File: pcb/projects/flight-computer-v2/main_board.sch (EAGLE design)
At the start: 110 parts, among them J1 B4B-PH-K-S(LF)(SN), J2 B4B-PH-K-S(LF)(SN), J3 B4B-PH-K-S(LF)(SN), J4 B4B-PH-K-S(LF)(SN), J5 B4B-PH-K-S(LF)(SN), J6 B4B-PH-K-S(LF)(SN), J7 104031-0811, J8 B4B-PH-K-S(LF)(SN), J9 U.FL-R-SMT(10), U1 COM-13909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

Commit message: updates to layout
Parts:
- removed C16: 0.01uF, rcl:C-EUC0603
- removed C2, C3, C4, C5: 0.1uF, rcl:C-EUC0603
- removed R1, R3, R4: 100k, microbuilder:RESISTOR_0603_NOOUT
- removed U$3: IRF7313PBF, COM-13909:IRF7313PBF
- removed U$34: MAX3232E, TI_radio:MAX3232E
- added JP2: (no value), pinhead:PINHD-1X4
- added SJ10, SJ11, SJ8: (no value), jumper:SJ2W
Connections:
- removed net 3.3V: C4.1, U$34.VCC
- removed net EN: JP3.2, R45.2, U13.EN
- removed net GATE_GPS: JP3.9, R4.1, U$3.G1
- removed net GND_CONVERTERS: U$1.D1@1, U$1.D1@2
- removed net GND_GPS: J2.4, U$3.D1@1, U$3.D1@2
- removed net GND_RADIO: U$3.D2@1, U$3.D2@2, U1.GND
- removed net N$1: R5.2, R6.2
- removed net N$10: C2.2, U$34.C1-
- removed net N$17: C5.2, U$34.C2-
- removed net N$18: C16.1, U$34.V-
- removed net N$19: C3.1, U$34.V+
- removed net SCL1: U10.SCL, U4.SCL, U5.SCL, U7.SCL, U8.SCL, U9.SCL
- removed net SDA1: U10.SDA, U4.SDA, U5.SDA, U7.SDA, U8.SDA, U9.SDA
- new net 3V32_CTRL: JP3.9, R45.2, U13.EN
- net 3V3: now also SJ8.1; no longer C7.2, U$2.VCC
- net 3V32: now also SJ8.3
- net 5V: now also JP2.4, SJ10.3, SJ11.3; no longer J2.3, J4.3
- net GATE_IRIDIUM: no longer R1.1
- net GATE_PI: now also R5.1, U$5.G1; no longer R6.1, U$5.G2
- net GATE_RADIO: no longer R3.1, U$3.G2
- net GATE_SPEC: now also R6.1, U$5.G2; no longer R5.1, U$5.G1
- net GND: now also JP2.1, R2.2, R5.2, R6.2, U1.GND; no longer C16.2, C3.2, C4.2, C9.1, U$2.GND, U$3.S1, U$3.S2, U$34.GND
- net GND_IRIDIUM: now also C9.1, J2.4, U$1.D1@1, U$1.D1@2, U$2.GND
- net GND_PI: now also U$5.D1@1, U$5.D1@2; no longer U$5.D2@1, U$5.D2@2
- net GND_SPEC: now also U$5.D2@1, U$5.D2@2; no longer U$5.D1@1, U$5.D1@2
- net N$16: now also J4.3, SJ11.2; no longer C5.1, U$34.C2+
- net N$6: now also J2.3, SJ10.2; no longer R1.2, R2.2, R3.2, R4.2
- net N$9: now also C7.2, SJ8.2, U$2.VCC; no longer C2.1, U$34.C1+
- net R232: no longer U$34.RI2
- net R232_GPS: no longer U$34.RI1
- net RGPS: no longer U$34.RO1
- net RIRI: no longer U$34.RO2
- net SCL: now also U10.SCL, U4.SCL, U5.SCL, U7.SCL, U8.SCL, U9.SCL
- net SDA: now also U10.SDA, U4.SDA, U5.SDA, U7.SDA, U8.SDA, U9.SDA
- net T232: no longer U$34.DO2
- net T232_GPS: no longer U$34.DO1
- net TGPS: no longer U$34.DI1
- net TIRI: no longer U$34.DI2
- net VBAT: now also JP2.3
- net VIN: now also JP2.2, SJ10.1, SJ11.1
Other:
- note removed: "Backup Serial Converter"
- note removed: "RS232 Connections"

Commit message: update PCB and libraries
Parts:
- added JP4: (no value), pinhead:PINHD-1X2
- added R1, R9: 10k, rcl:R-EU_R0603
- added R3: 7.5k, rcl:R-EU_R0603
- added R4: 4.3k, rcl:R-EU_R0603
- added SJ9: (no value), jumper:SJ
- renumbered U$1 to U12, U$2 to U11, U$5 to U14
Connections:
- removed net GND_I2C: J3.4
- new net N$1: JP4.1, SJ9.1, U1.3.3V
- new net N$10: R1.2, R3.2, U8.ADDR
- new net N$17: R4.2, R9.2, U7.ADDR
- net 3V3: now also R1.1, R9.1, U6.AP_CS; no longer U8.ADDR
- net 3V32: now also JP4.2, SJ9.2; no longer U1.3.3V
- net GND: now also C9.1, J3.4, R3.1, R4.1, U11.GND, U6.FSYNC; no longer U7.ADDR
- net GND_IRIDIUM: no longer C9.1, U11.GND
- net N$3: now also SJ2.2; no longer SJ1.2
- net N$4: now also SJ1.2; no longer SJ2.2
- net SCL: now also U6.AP_SCL/AP_SCLK
- net SDA: now also U6.AP_SDA/AP_SDIO/AP_SDI

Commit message: update libraries and v2 flight comp
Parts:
- added JP5: (no value), pinhead:PINHD-1X2
- added JP6: (no value), pinhead:PINHD-1X4
- added JP7: (no value), pinhead:PINHD-1X3
- added LED1, LED2, LED3, LED4: (no value), adafruit:LEDCHIPLED_0603
- added R10, R11, R12, R27: (no value), rcl:R-US_R0603
- added U3: IRF7313PBF, COM-13909:IRF7313PBF
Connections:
- removed net GATE_RADIO: JP1.12
- new net BOOTN: JP6.3, U$4.BOOTN
- new net EXT_INT: JP1.12, JP5.1
- new net H3_INT1: JP7.2, U2.INT1
- new net H3_INT2: JP7.3, U2.INT2
- new net HINTN: JP6.4, U$4.HINTN
- new net N$19: LED1.A, R10.2
- new net PS1: JP6.2, U$4.PS1
- new net VIN_GND: J5.1, U3.D1@1, U3.D1@2, U3.D2@1, U3.D2@2
- net 3V32_CTRL: now also R27.1
- net FSM300_RESET: now also JP6.1
- net GATE_IRIDIUM: now also R10.1, U3.G1, U3.G2
- net GATE_PI: now also R11.1
- net GATE_SPEC: now also R12.1
- net GND: now also JP5.2, LED1.C, LED2.C, LED3.C, LED4.C, U$4.PS0_WAKEN, U3.S1, U3.S2; no longer J5.2
- net ICM_INT: now also JP7.1
- net N$33: now also LED2.A, R11.2; no longer U$4.HINTN
- net N$36: now also LED3.A, R12.2; no longer U$4.BOOTN
- net N$37: now also LED4.A, R27.2; no longer U$4.PS1
- net VIN: now also J5.2; no longer J5.1

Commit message: v2 cam files, renderings, and datasheets
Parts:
- added C2: 0.1uF, rcl:C-EUC0603
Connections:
- net GND: now also C2.1, C7.1
- net N$11: now also C7.2; no longer C7.1
- net N$9: now also C2.2; no longer C7.2
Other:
- note added: "POL mosfet for J2 and J4"
- moved on the sheet: C7
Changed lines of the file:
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@@
 <part name="R12" library="rcl" library_urn="urn:adsk.eagle:library:334" deviceset="R-US_" device="R0603" package3d_urn="urn:adsk.eagle:package:23555/3"/>
 <part name="R27" library="rcl" library_urn="urn:adsk.eagle:library:334" deviceset="R-US_" device="R0603" package3d_urn="urn:adsk.eagle:package:23555/3"/>
+<part name="C2" library="rcl" library_urn="urn:adsk.eagle:library:334" deviceset="C-EU" device="C0603" package3d_urn="urn:adsk.eagle:package:23616/2" value="0.1uF"/>
 </parts>
 <sheets>
@@
 <wire x1="154.94" y1="101.6" x2="248.92" y2="101.6" width="0.254" layer="94"/>
 <text x="165.1" y="104.14" size="3.81" layer="94">Mounting holes</text>
+<text x="127" y="88.9" size="3.81" layer="94">POL mosfet for J2 and J4</text>
 </plain>
 <instances>
@@
 <attribute name="VALUE" x="176.276" y="167.259" size="1.778" layer="96" rot="R180"/>
 </instance>
-<instance part="C7" gate="G$1" x="213.36" y="177.8" smashed="yes" rot="R90">
-<attribute name="NAME" x="212.979" y="179.324" size="1.778" layer="95" rot="R90"/>
-<attribute name="VALUE" x="218.059" y="179.324" size="1.778" layer="96" rot="R90"/>
+<instance part="C7" gate="G$1" x="190.5" y="175.26" smashed="yes" rot="R90">
+<attribute name="NAME" x="190.119" y="176.784" size="1.778" layer="95" rot="R90"/>
+<attribute name="VALUE" x="195.199" y="176.784" size="1.778" layer="96" rot="R90"/>
 </instance>
 <instance part="C8" gate="G$1" x="177.8" y="152.4" smashed="yes" rot="R180">
@@
 <attribute name="NAME" x="147.32" y="78.74" size="1.27" layer="95"/>
 <attribute name="VALUE" x="157.48" y="78.74" size="1.27" layer="96"/>
+</instance>
+<instance part="C2" gate="G$1" x="223.52" y="177.8" smashed="yes" rot="R90">
+<attribute name="NAME" x="223.139" y="179.324" size="1.778" layer="95" rot="R90"/>
+<attribute name="VALUE" x="228.219" y="179.324" size="1.778" layer="96" rot="R90"/>
 </instance>
 </instances>
@@
 <label x="127" y="68.58" size="1.778" layer="95"/>
 </segment>
+<segment>
+<pinref part="C7" gate="G$1" pin="1"/>
+<wire x1="187.96" y1="175.26" x2="182.88" y2="175.26" width="0.1524" layer="91"/>
+<label x="177.8" y="175.26" size="1.778" layer="95"/>
+</segment>
+<segment>
+<pinref part="C2" gate="G$1" pin="1"/>
+<wire x1="220.98" y1="177.8" x2="218.44" y2="177.8" width="0.1524" layer="91"/>
+<label x="215.9" y="177.8" size="1.778" layer="95"/>
+</segment>
 </net>
 <net name="RIRI" class="0">
@@
 <segment>
 <pinref part="U11" gate="G$1" pin="V+"/>
-<wire x1="200.66" y1="165.1" x2="198.12" y2="165.1" width="0.1524" layer="91"/>
-<pinref part="C7" gate="G$1" pin="1"/>
-<wire x1="198.12" y1="165.1" x2="198.12" y2="177.8" width="0.1524" layer="91"/>
-<wire x1="198.12" y1="177.8" x2="210.82" y2="177.8" width="0.1524" layer="91"/>
+<pinref part="C7" gate="G$1" pin="2"/>
+<wire x1="195.58" y1="175.26" x2="195.58" y2="165.1" width="0.1524" layer="91"/>
+<wire x1="195.58" y1="165.1" x2="200.66" y2="165.1" width="0.1524" layer="91"/>
 </segment>
 </net>
@@
 <pinref part="SJ8" gate="G$1" pin="2"/>
 <wire x1="233.68" y1="177.8" x2="233.68" y2="167.64" width="0.1524" layer="91"/>
-<pinref part="C7" gate="G$1" pin="2"/>
-<wire x1="233.68" y1="177.8" x2="218.44" y2="177.8" width="0.1524" layer="91"/>
+<pinref part="C2" gate="G$1" pin="2"/>
+<wire x1="228.6" y1="177.8" x2="233.68" y2="177.8" width="0.1524" layer="91"/>
 <junction x="233.68" y="177.8"/>
 </segment>

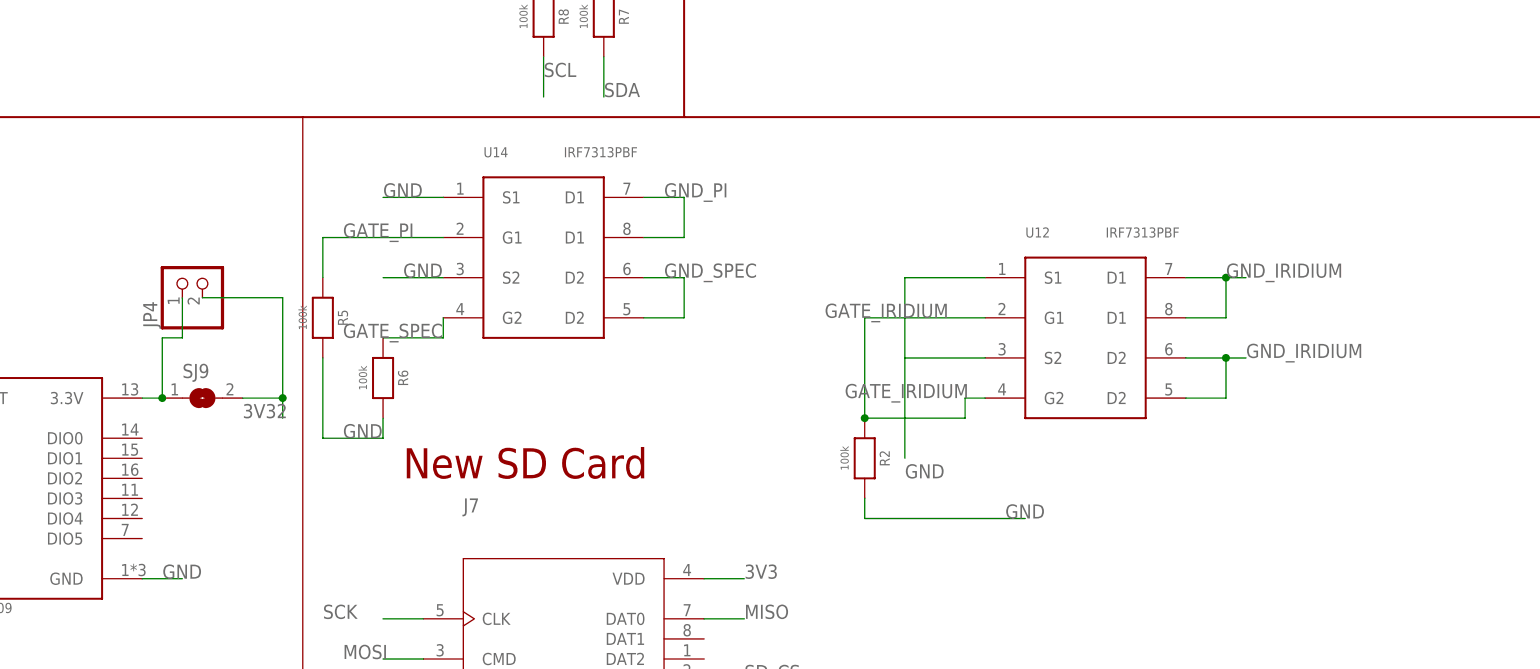
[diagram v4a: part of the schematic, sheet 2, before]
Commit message: add ssr to flight computer. add to hardware manual
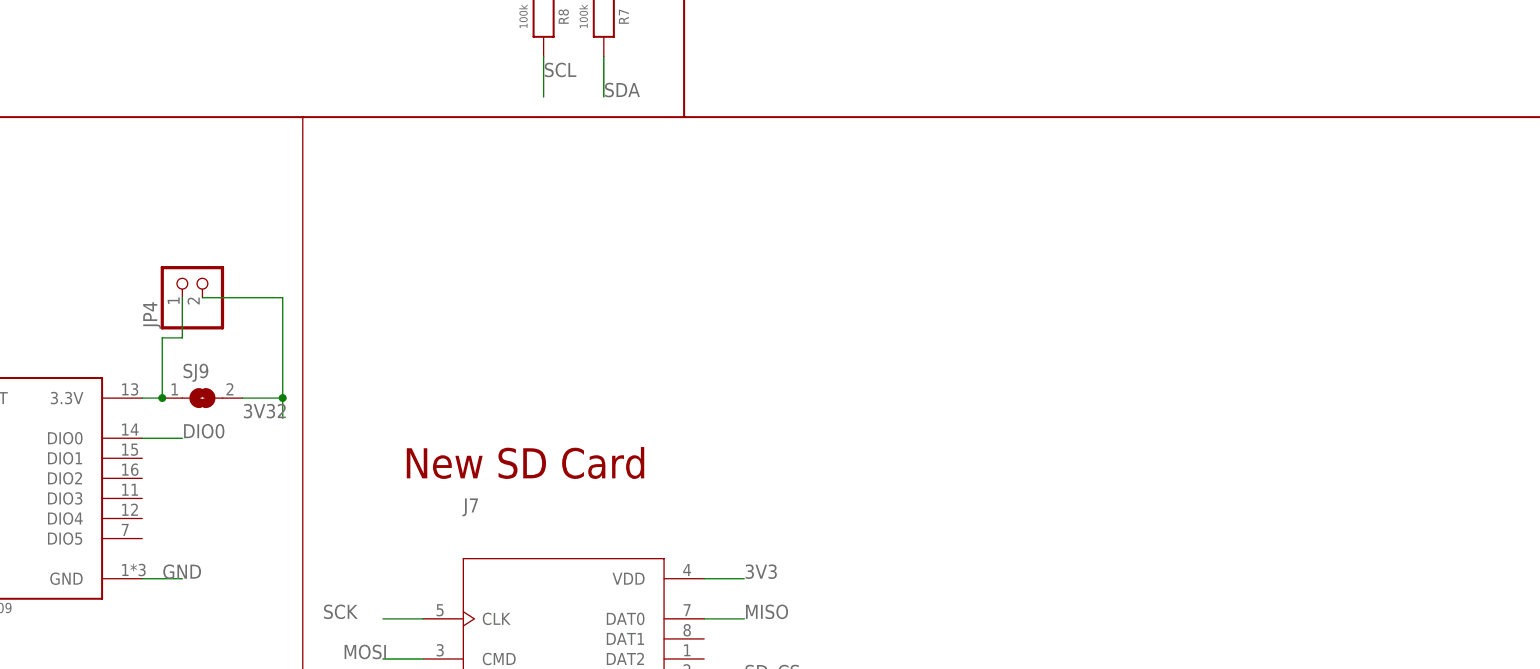
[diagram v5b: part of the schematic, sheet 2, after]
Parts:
- removed R5, R6: 100k, microbuilder:RESISTOR_0603_NOOUT
- removed U12, U14: IRF7313PBF, COM-13909:IRF7313PBF
- added C3: 0.1uF, rcl:C-EUC0603
- R2: value 100k -> 288
- U3: value IRF7313PBF -> AQV252G; device COM-13909:IRF7313PBF -> AQV252G:AQV252G
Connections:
- removed net VIN_GND: J5.1, U3.D1@1, U3.D1@2, U3.D2@1, U3.D2@2
- new net DIO0: U1.DIO0
- new net N$18: C3.2, R2.2, U3.LED+
- new net VIN_PRE: J5.2, U3.SW+1
- net GATE_IRIDIUM: no longer U12.G1, U12.G2, U3.G1, U3.G2
- net GATE_PI: no longer R5.1, U14.G1
- net GATE_SPEC: no longer R6.1, U14.G2
- net GND: now also C3.1, J5.1, U3.LED-; no longer R2.2, R5.2, R6.2, U12.S1, U12.S2, U14.S1, U14.S2, U3.S1, U3.S2
- net GND_IRIDIUM: no longer U12.D1@1, U12.D1@2, U12.D2@1, U12.D2@2
- net GND_PI: no longer U14.D1@1, U14.D1@2
- net GND_SPEC: no longer U14.D2@1, U14.D2@2
- net VIN: now also U3.SW+2; no longer J5.2
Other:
- note removed: "POL mosfet for J2 and J4"
